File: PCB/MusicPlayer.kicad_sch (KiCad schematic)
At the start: 0 parts

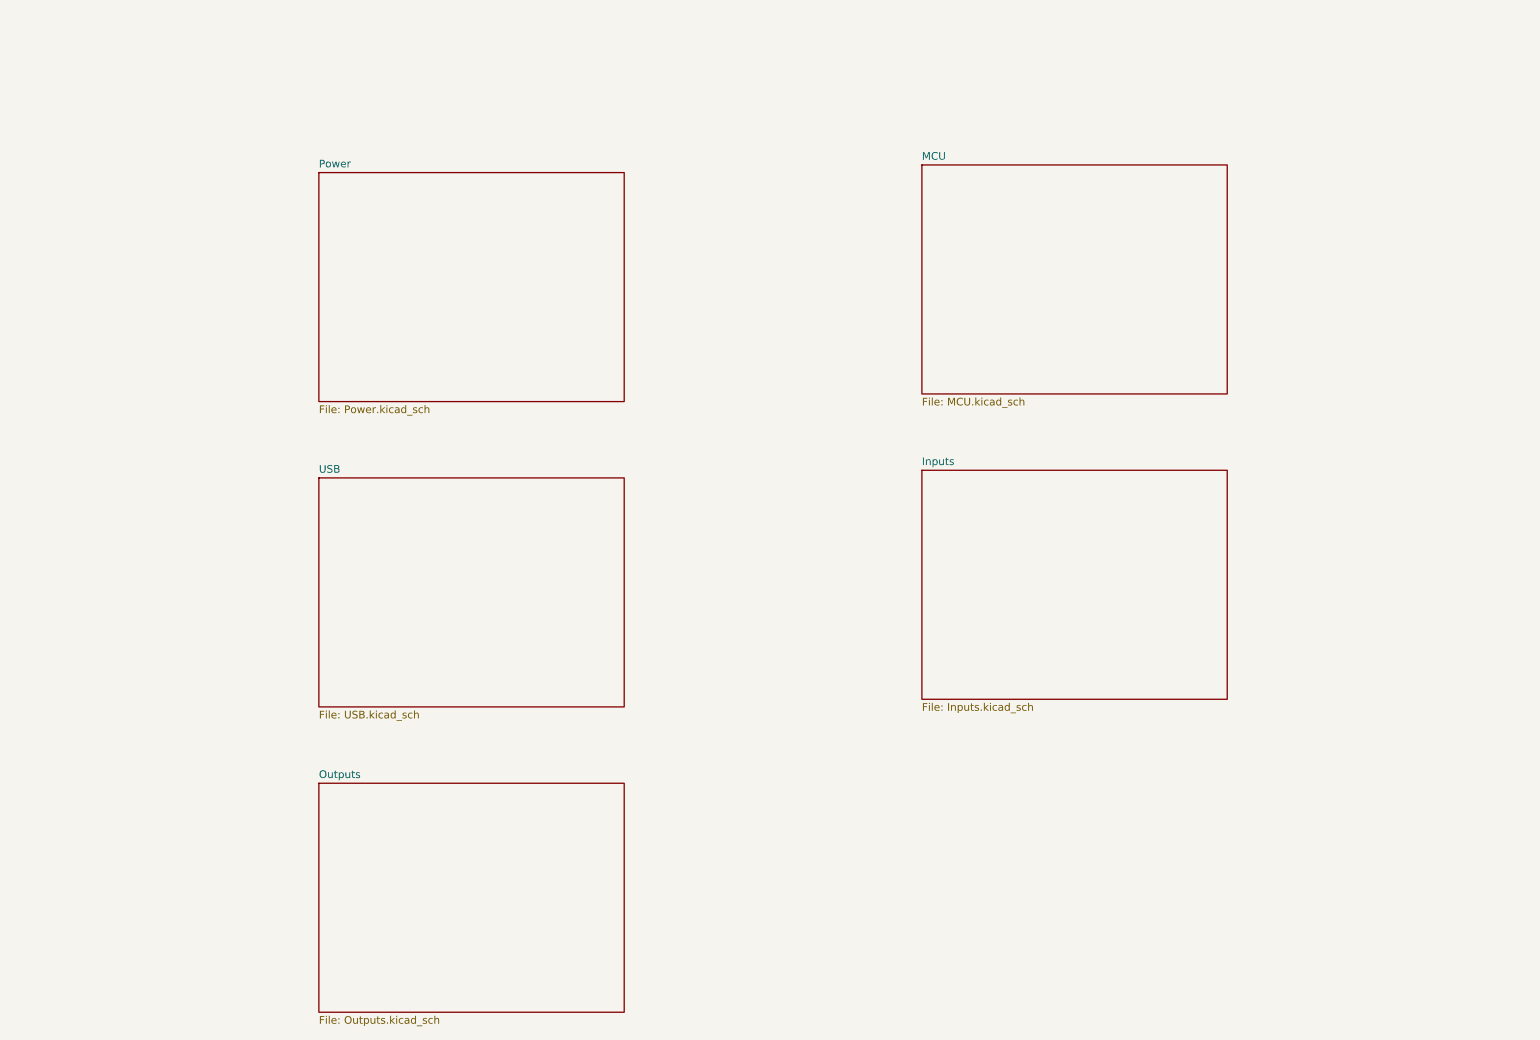
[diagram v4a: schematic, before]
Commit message: Update Power schematic with new symbols and components
Replaced and added several symbols in Power.kicad_sch, including MCP73831-2-OT battery charger, TPS61090 boost converter, and updated passive components (LED, capacitor, inductor, resistor). Adjusted symbol properties, footprints, and pinouts to match new components. Updated schematic text, junctions, and added descriptive notes for charge rate and low battery voltage. Minor tweaks to MusicPlayer.kicad_sch sheet positions and grouping in MusicPlayer.kicad_pro.
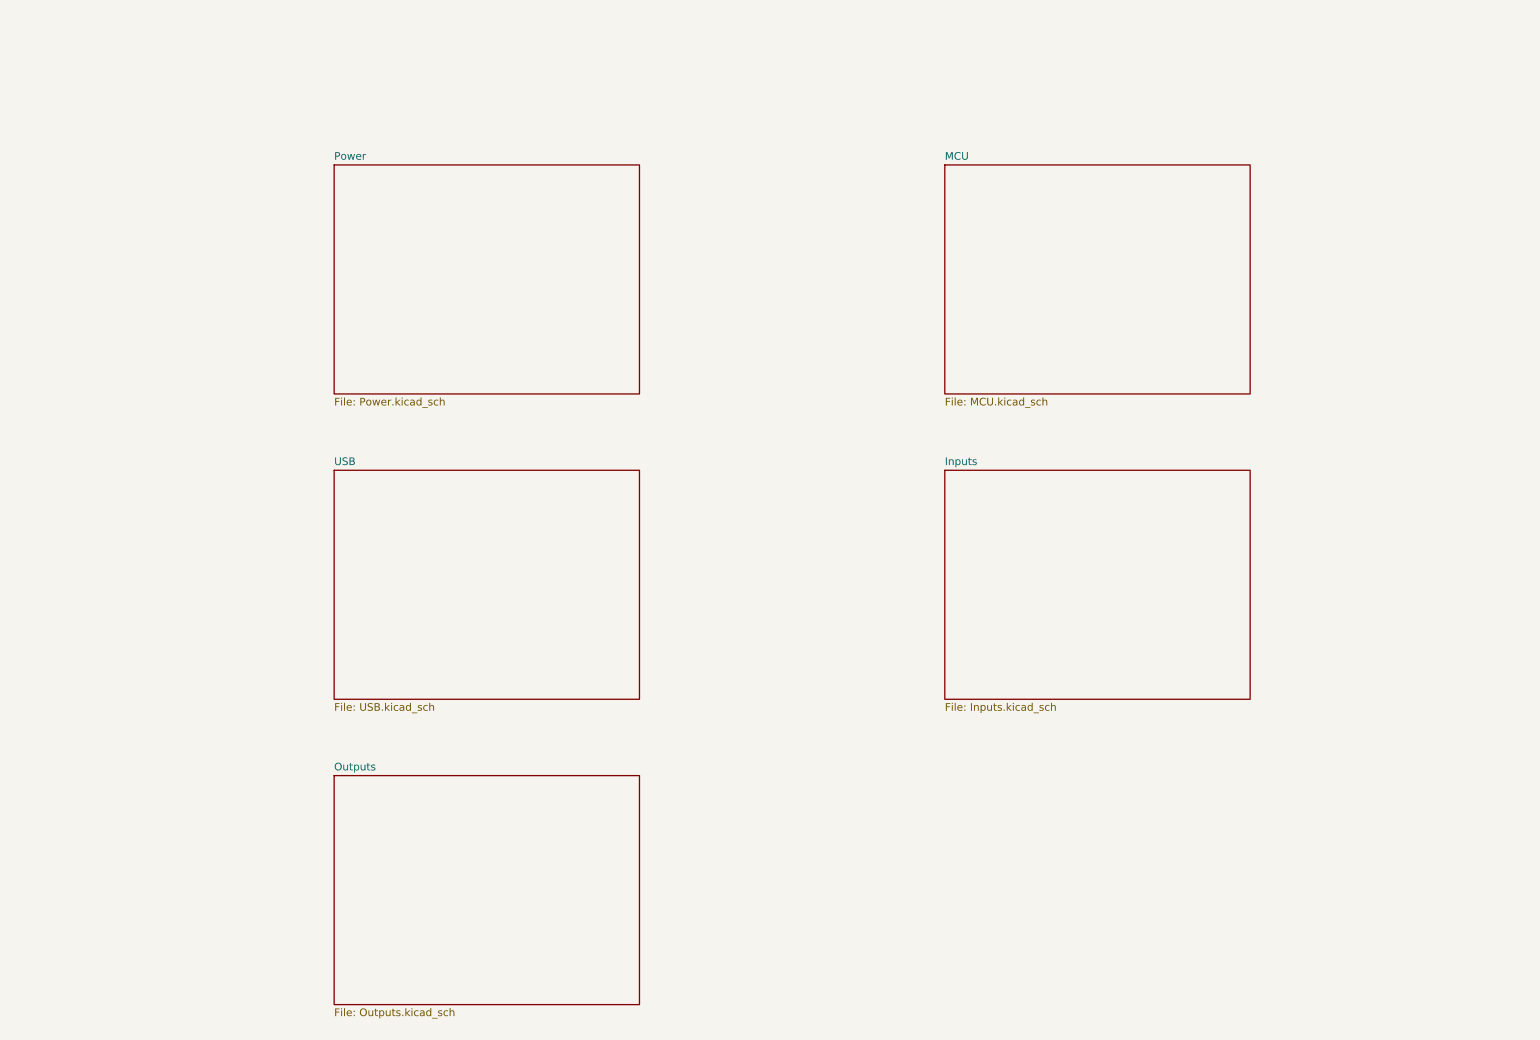
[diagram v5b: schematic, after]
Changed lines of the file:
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@@
 	)
 	(sheet
-		(at 161.29 38.1)
+		(at 165.1 38.1)
 		(size 50.8 38.1)
 		(exclude_from_sim no)
@@
 		)
 		(property "Sheetname" "MCU"
-			(at 161.29 37.3884 0)
+			(at 165.1 37.3884 0)
 			(effects
 				(font
@@
 		)
 		(property "Sheetfile" "MCU.kicad_sch"
-			(at 161.29 76.7846 0)
+			(at 165.1 76.7846 0)
 			(effects
 				(font
@@
 	)
 	(sheet
-		(at 60.96 39.37)
+		(at 63.5 38.1)
 		(size 50.8 38.1)
 		(exclude_from_sim no)
@@
 		)
 		(property "Sheetname" "Power"
-			(at 60.96 38.6584 0)
+			(at 63.5 37.3884 0)
 			(effects
 				(font
@@
 		)
 		(property "Sheetfile" "Power.kicad_sch"
-			(at 60.96 78.0546 0)
+			(at 63.5 76.7846 0)
 			(effects
 				(font
@@
 	)
 	(sheet
-		(at 161.29 88.9)
+		(at 165.1 88.9)
 		(size 50.8 38.1)
 		(exclude_from_sim no)
@@
 		)
 		(property "Sheetname" "Inputs"
-			(at 161.29 88.1884 0)
+			(at 165.1 88.1884 0)
 			(effects
 				(font
@@
 		)
 		(property "Sheetfile" "Inputs.kicad_sch"
-			(at 161.29 127.5846 0)
+			(at 165.1 127.5846 0)
 			(effects
 				(font
@@
 	)
 	(sheet
-		(at 60.96 90.17)
+		(at 63.5 88.9)
 		(size 50.8 38.1)
 		(exclude_from_sim no)
@@
 		)
 		(property "Sheetname" "USB"
-			(at 60.96 89.4584 0)
+			(at 63.5 88.1884 0)
 			(effects
 				(font
@@
 		)
 		(property "Sheetfile" "USB.kicad_sch"
-			(at 60.96 128.8546 0)
+			(at 63.5 127.5846 0)
 			(effects
 				(font
@@
 	)
 	(sheet
-		(at 60.96 140.97)
+		(at 63.5 139.7)
 		(size 50.8 38.1)
 		(exclude_from_sim no)
@@
 		)
 		(property "Sheetname" "Outputs"
-			(at 60.96 140.2584 0)
+			(at 63.5 138.9884 0)
 			(effects
 				(font
@@
 		)
 		(property "Sheetfile" "Outputs.kicad_sch"
-			(at 60.96 179.6546 0)
+			(at 63.5 178.3846 0)
 			(effects
 				(font

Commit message: Finished the schematic.
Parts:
- added H1, H2, H3, H4: MountingHole, MountingHole:MountingHole_2.2mm_M2, symbol Mechanical:MountingHole

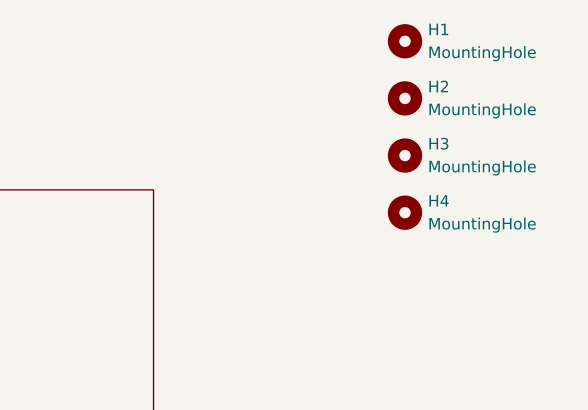
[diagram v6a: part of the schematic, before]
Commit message: Finished making a PCB for it
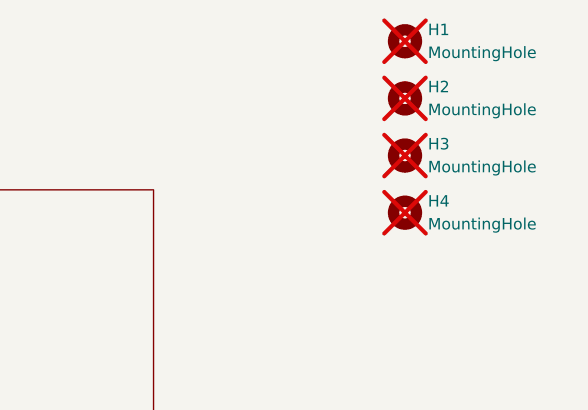
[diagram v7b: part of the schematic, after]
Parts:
- H1, H2, H3, H4: now not fitted
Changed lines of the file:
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@@
 		(in_bom no)
 		(on_board yes)
-		(dnp no)
+		(dnp yes)
 		(fields_autoplaced yes)
 		(property "Reference" "H2"
@@
 		(in_bom no)
 		(on_board yes)
-		(dnp no)
+		(dnp yes)
 		(fields_autoplaced yes)
 		(property "Reference" "H4"
@@
 		(in_bom no)
 		(on_board yes)
-		(dnp no)
+		(dnp yes)
 		(fields_autoplaced yes)
 		(property "Reference" "H3"
@@
 		(in_bom no)
 		(on_board yes)
-		(dnp no)
+		(dnp yes)
 		(fields_autoplaced yes)
 		(property "Reference" "H1"
